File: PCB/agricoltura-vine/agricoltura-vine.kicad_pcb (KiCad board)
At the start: 2 copper layers, 110 x 70 mm, 106 parts, among them SW1 B3U-1000P, SW2 CVS-02TB, SW3 CVS-02TB, SW4 CVS-02TB, SW5 CVS-02TB, T1 BU2032SM-JJ-GTR, T10 B4B-PH-K-S(LF)(SN), T11 B4B-PH-K-S(LF)(SN), T12 B4B-PH-K-S(LF)(SN), T13 B4B-PH-K-S(LF)(SN), T14 B4B-PH-K-S(LF)(SN), T15 B4B-PH-K-S(LF)(SN), T16 1755736, T17 RJHSE-5381, T18 RJHSE-5381, T19 TSW-108-07-G-T, T2 20021121-00010C4LF, T20 TSW-108-07-G-T, T3 0675031020, T4 B4B-PH-K-S(LF)(SN), T5 B4B-PH-K-S(LF)(SN), T6 B4B-PH-K-S(LF)(SN), T7 B4B-PH-K-S(LF)(SN), T8 B4B-PH-K-S(LF)(SN), T9 B4B-PH-K-S(LF)(SN), U1 STM32F446RET6, U2 74HC4052D, U3 TCA9548APWR, U4 AP63203WU-7, U5 AP63205WU-7, U6 MAX3073EESD+, U7 MAX3073EESD+, U8 SN74LV541APWR, U9 TXB0108PWR, X1 ABM3B-8.000MHZ-B2-T, X2 ABS07-32.768KHZ-9-T

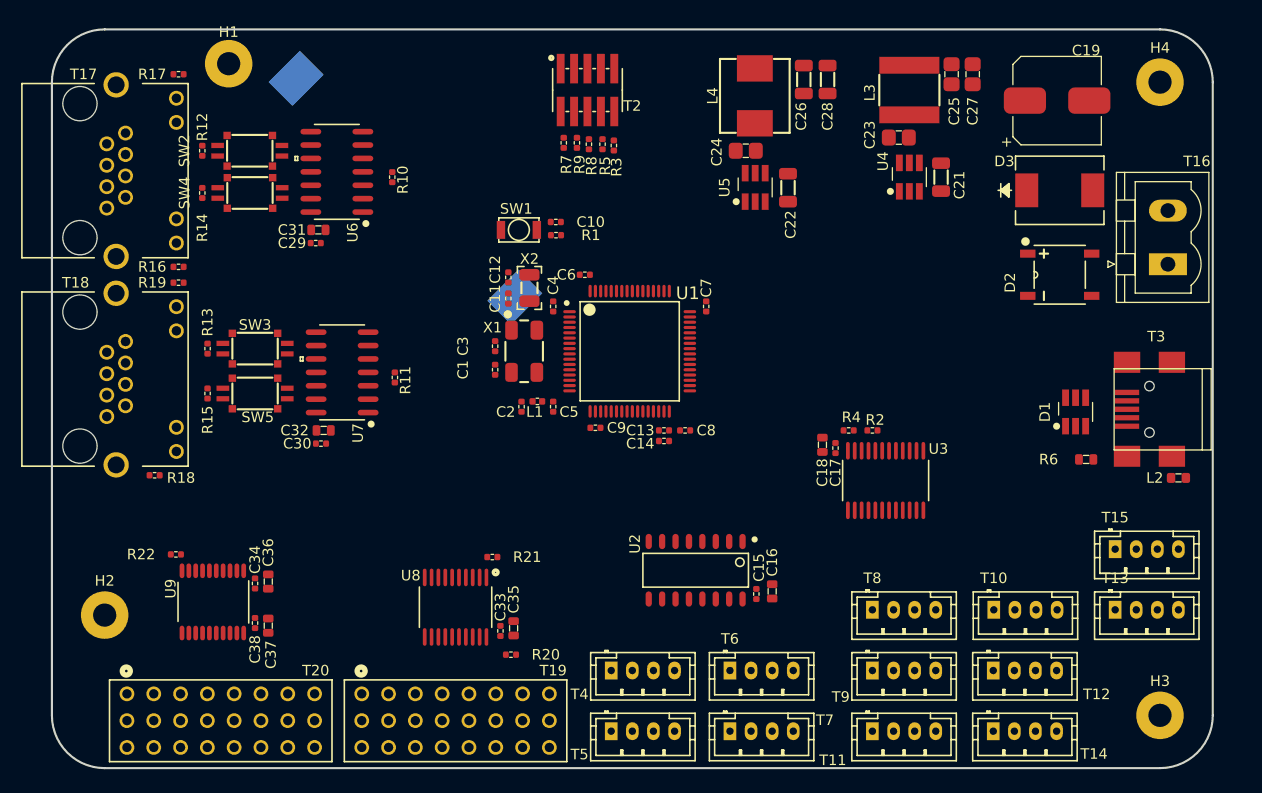
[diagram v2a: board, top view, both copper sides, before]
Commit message: Route Started Connectors Changed
Changed to QWIIC style connectors and adjusted pinning of RJ45s, but switching to screw terminal header in next commit. THis is a backup
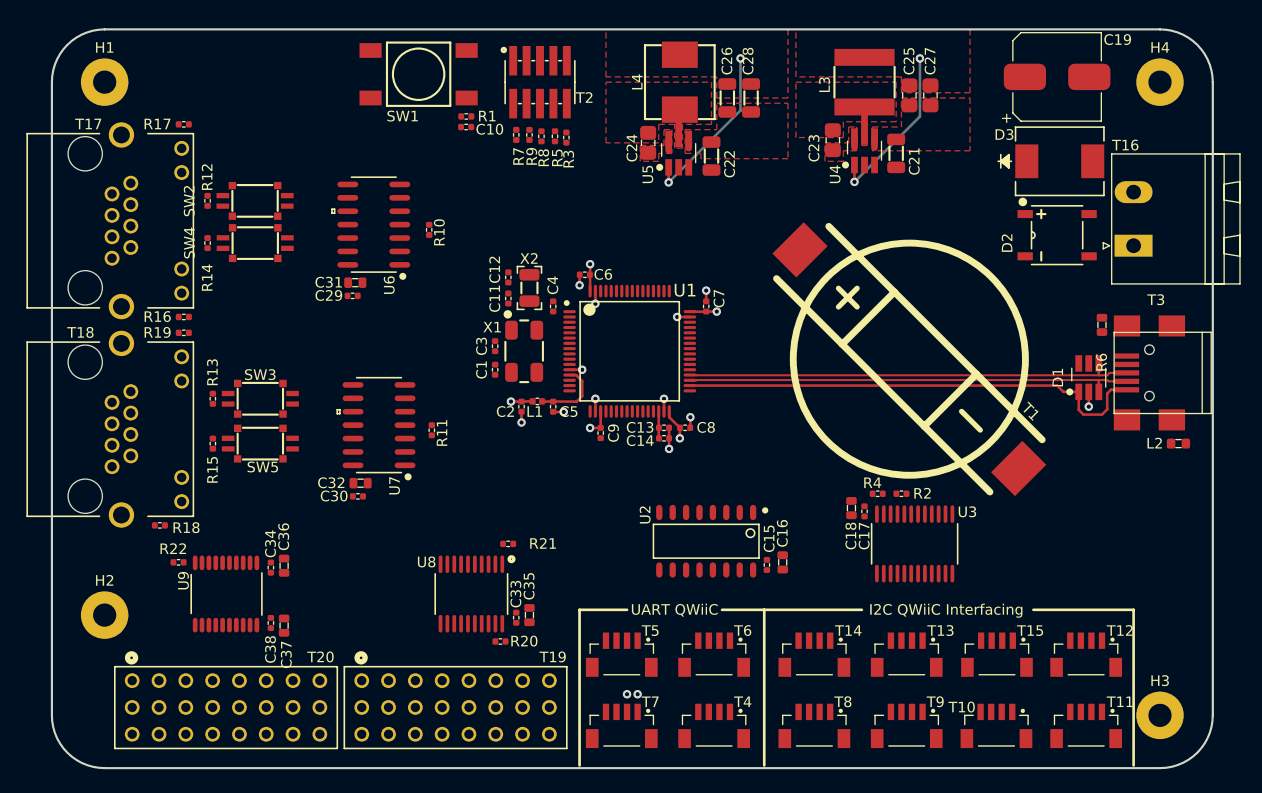
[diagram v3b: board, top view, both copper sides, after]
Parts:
- SW1: value B3U-1000P -> TL3301NF260QG; footprint AVR-KiCAD-Lib-Mech-Switches:B3U-1000P -> AVR-KiCAD-Lib-Mech-Switches:TL3301NF260QG
- T1: moved to F.Cu
- T10, T11, T12, T13, T14, T15, T4, T5, T6, T7, T8, T9: value B4B-PH-K-S(LF)(SN) -> BM04B-SRSS-TB(LF)(SN); footprint AVR-KiCAD-Lib-Connectors:B4B-PH-K-S(LF)(SN) -> AVR-KiCAD-Lib-Connectors:CONN_BM04B-SRSS-TB(LF)(SN)
- T16: value 1755736 -> 1757242; footprint growbox-KiCAD-Connectors:PhoenixContact_MSTBVA-G_02x5.08mm_Vertical -> AVR-KiCAD-Lib-Connectors:PhoenixContact_MSTBA-G_02x5.08mm_Angled
- moved T1 50.4 mm to (186.2, 96.2), turned to 315 degrees
- moved T11 20.3 mm to (203.0, 131.0), turned to 180 degrees
- moved T13 20.2 mm to (186.0, 124.2), turned to 180 degrees
- moved T14 18.4 mm to (177.2, 124.2), turned to 180 degrees
- moved SW1 17.5 mm to (139.8, 69.2)
- moved T15 15.0 mm to (194.6, 124.2), turned to 180 degrees
- moved R1 14.1 mm to (144.3, 73.2)
- moved R6 12.8 mm to (204.5, 93.0), turned to 90 degrees
- moved C10 12.4 mm to (144.2, 74.2), turned to 0 degrees
- moved T8 12.3 mm to (177.2, 131.0), turned to 180 degrees
- moved H1 11.9 mm to (110.0, 70.0)
- moved T4 11.1 mm to (167.8, 131.0), turned to 180 degrees
- moved T10 11.0 mm to (194.5, 131.0), turned to 180 degrees
- moved T7 10.3 mm to (159.0, 131.0), turned to 180 degrees
- moved C24 9.28 mm to (161.5, 75.8), turned to 90 degrees
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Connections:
- net Net-(C1-Pad1) renamed /STM32F446RET Controller/OSC_IN
- net Net-(C11-Pad2) renamed /STM32F446RET Controller/OSC32_OUT
- net Net-(C12-Pad2) renamed /STM32F446RET Controller/OSC32_IN
- net Net-(C13-Pad1) renamed /STM32F446RET Controller/VCAP1
- net Net-(C3-Pad1) renamed /STM32F446RET Controller/OSC_OUT
- net Net-(D1-Pad1) renamed /STM32F446RET Controller/VBUS
- net Net-(D1-Pad3) renamed /STM32F446RET Controller/D-
- net Net-(D1-Pad4) renamed /STM32F446RET Controller/D+
- net Net-(D1-Pad6) renamed /STM32F446RET Controller/ID
- net Net-(T4-Pad1) renamed /UART Sensor Interfaces/UARTS1_RX
- net Net-(T4-Pad2) renamed /UART Sensor Interfaces/UARTS1_TX
- net Net-(T5-Pad1) renamed /UART Sensor Interfaces/UARTS2_RX
- net Net-(T5-Pad2) renamed /UART Sensor Interfaces/UARTS2_TX
- net Net-(T6-Pad1) renamed /UART Sensor Interfaces/UARTS3_RX
- net Net-(T6-Pad2) renamed /UART Sensor Interfaces/UARTS3_TX
- net Net-(T7-Pad1) renamed /UART Sensor Interfaces/UARTS4_RX
- net Net-(T7-Pad2) renamed /UART Sensor Interfaces/UARTS4_TX
- C10 pad 1: Net-(C10-Pad1) -> /STM32F446RET Controller/NRST
- R1 pad 2: Net-(C10-Pad1) -> /STM32F446RET Controller/NRST
- SW1 pad 1: Net-(C10-Pad1) -> /STM32F446RET Controller/NRST
- SW1 pad 2: GND -> /STM32F446RET Controller/NRST
- SW2 pad 1: Net-(R12-Pad1) -> Net-(R12-Pad2)
- SW2 pad 2: Net-(R12-Pad2) -> Net-(R12-Pad1)
- SW3 pad 1: Net-(R13-Pad1) -> Net-(R13-Pad2)
- SW3 pad 2: Net-(R13-Pad2) -> Net-(R13-Pad1)
- SW4 pad 1: Net-(R14-Pad1) -> Net-(R14-Pad2)
- SW4 pad 2: Net-(R14-Pad2) -> Net-(R14-Pad1)
- SW5 pad 1: Net-(R15-Pad1) -> Net-(R15-Pad2)
- SW5 pad 2: Net-(R15-Pad2) -> Net-(R15-Pad1)
- T17 pad 2: Net-(SW2-Pad3) -> Net-(SW4-Pad3)
- T17 pad 3: Net-(SW2-Pad4) -> Net-(SW4-Pad4)
- T17 pad 6: Net-(SW4-Pad3) -> Net-(SW2-Pad3)
- T17 pad 7: Net-(SW4-Pad4) -> Net-(SW2-Pad4)
- T18 pad 2: Net-(SW3-Pad3) -> Net-(SW5-Pad3)
- T18 pad 3: Net-(SW3-Pad4) -> Net-(SW5-Pad4)
- T18 pad 6: Net-(SW5-Pad3) -> Net-(SW3-Pad3)
- T18 pad 7: Net-(SW5-Pad4) -> Net-(SW3-Pad4)
- U1 pad 7: Net-(C10-Pad1) -> /STM32F446RET Controller/NRST
- U6 pad 10: Net-(SW2-Pad4) -> Net-(SW2-Pad3)
- U6 pad 11: Net-(SW4-Pad3) -> Net-(SW4-Pad4)
- U6 pad 12: Net-(SW4-Pad4) -> Net-(SW4-Pad3)
- U6 pad 9: Net-(SW2-Pad3) -> Net-(SW2-Pad4)
- U7 pad 10: Net-(SW3-Pad4) -> Net-(SW3-Pad3)
- U7 pad 11: Net-(SW5-Pad3) -> Net-(SW5-Pad4)
- U7 pad 12: Net-(SW5-Pad4) -> Net-(SW5-Pad3)
- U7 pad 9: Net-(SW3-Pad3) -> Net-(SW3-Pad4)
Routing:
- net /STM32F446RET Controller/VBUS: track 0.00 -> 45.4 mm
- net /STM32F446RET Controller/D+: track 0.00 -> 42.6 mm
- net /STM32F446RET Controller/D-: track 0.00 -> 42.6 mm
- net +3V3: track 0.00 -> 28.6 mm, vias 0 -> 7
- net GND: track 0.00 -> 16.4 mm, vias 0 -> 12
- net +5V: track 0.00 -> 16.0 mm, vias 0 -> 2
- net /STM32F446RET Controller/VDDA: track 0.00 -> 6.88 mm
- net Net-(C24-Pad2): track 0.00 -> 2.82 mm
- net Net-(C23-Pad2): track 0.00 -> 2.80 mm
- net /STM32F446RET Controller/VCAP1: track 0.00 -> 2.56 mm
- net Net-(C23-Pad1): track 0.00 -> 1.12 mm
- net Net-(C24-Pad1): track 0.00 -> 1.07 mm
- net /UART Sensor Interfaces/UARTS4_TX: vias 0 -> 1
- net /UART Sensor Interfaces/UARTS4_RX: vias 0 -> 1
- added copper zone on F.Cu, net +3V3
- added copper zone on F.Cu, net +5V
- added copper zone on F.Cu, net GND
- added copper zone on In1.Cu, net GND
- added copper zone on F.Cu, net Net-(C23-Pad1)
- added copper zone on F.Cu, net Net-(C23-Pad2)
- added copper zone on F.Cu, net Net-(C24-Pad1)
- added copper zone on F.Cu, net Net-(C24-Pad2)
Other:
- copper layers 2 -> 4
- rule trace_min: 0.2 -> 0.1778
- board text added: "I2C QWiiC Interfacing"
- board text added: "UART QWiiC"

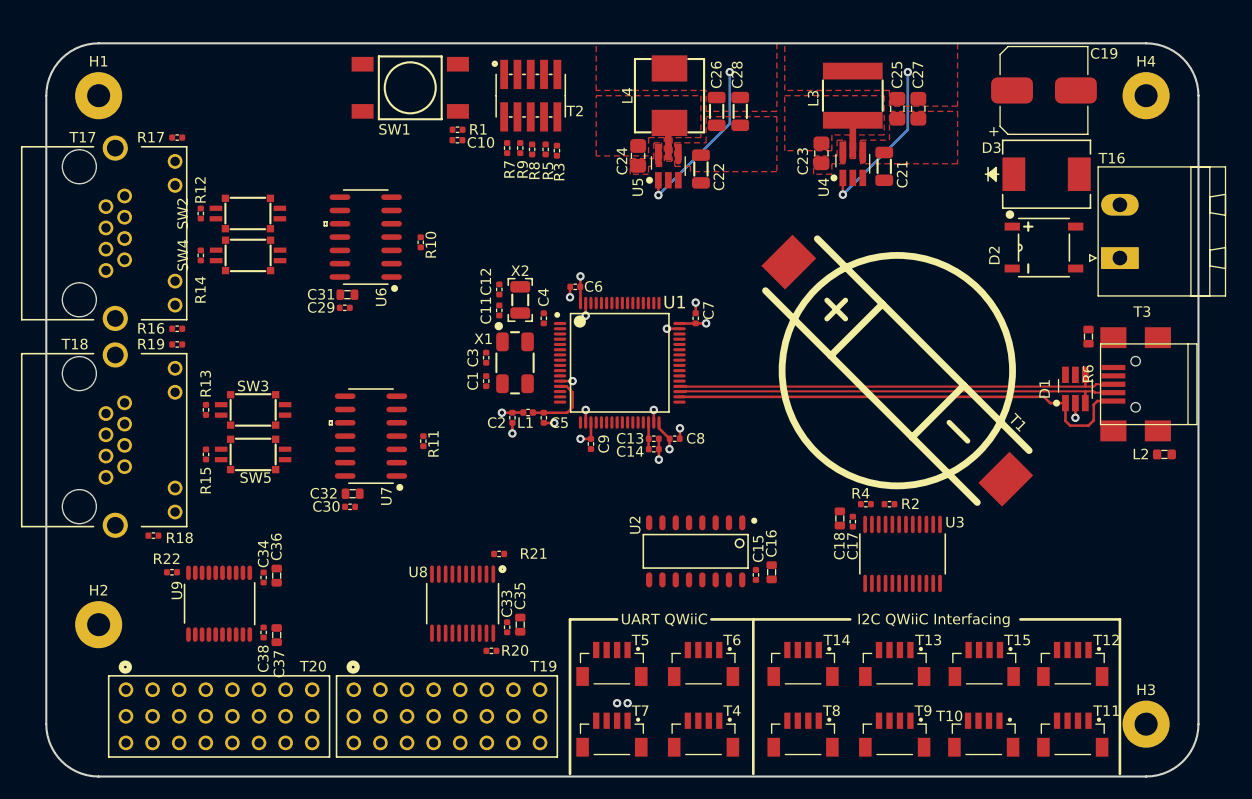
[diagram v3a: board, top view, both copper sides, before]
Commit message: Routing and New RS485
swapped over the RS485 chip to a new one and started routing the board.
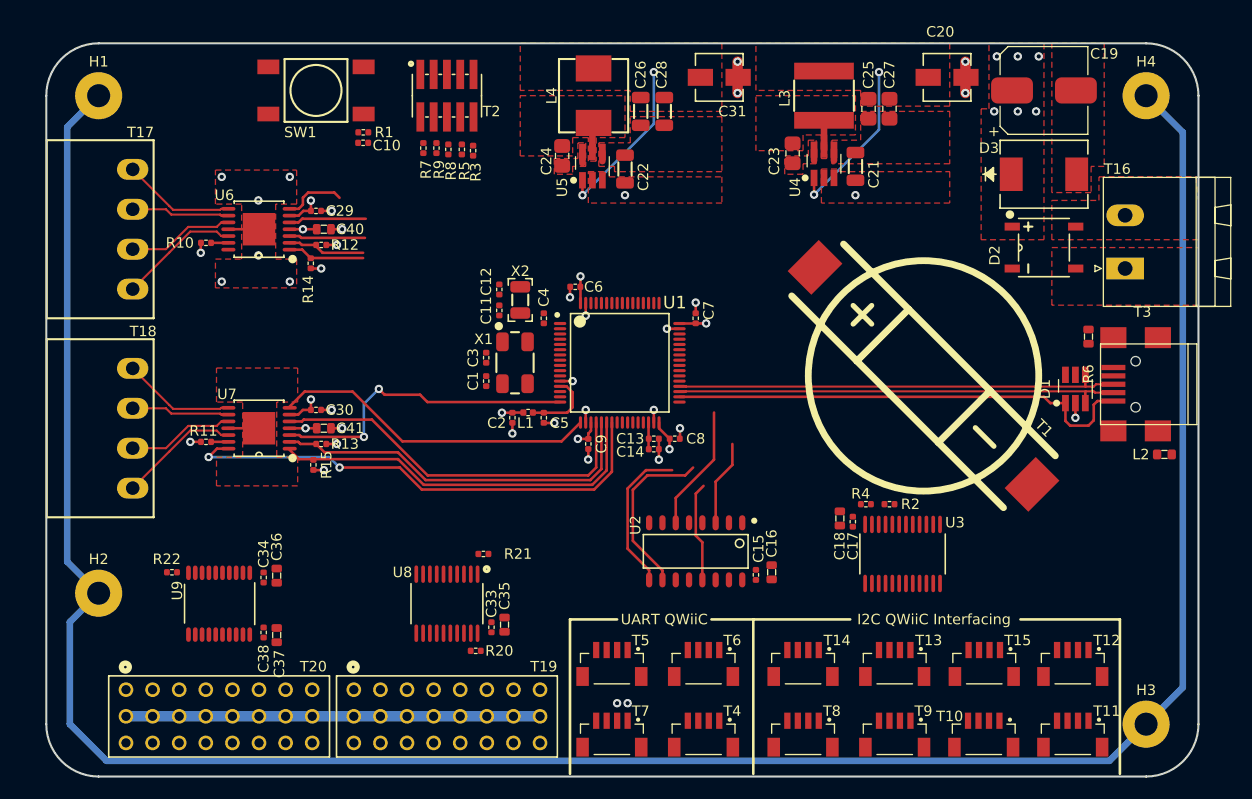
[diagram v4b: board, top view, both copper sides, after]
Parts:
- removed C32: GRM188R61A106KE69J, AVR-KiCAD-Lib-Capacitors:C0603
- removed R16, R17, R18, R19: RC0402FR-071KL, AVR-KiCAD-Lib-Resistors:R0402
- removed SW2, SW3, SW4, SW5: CVS-02TB, AVR-KiCAD-Lib-Mech-Switches:CVS-02TB
- added C20: UCM1C470MCL1GS, AVR-KiCAD-Lib-Capacitors:UCM1C470MCL1GS, F.Cu at (191.0, 68.2)
- added C40: CGA3E2X7R1H104K080AA, AVR-KiCAD-Lib-Capacitors:C0603, F.Cu at (131.5, 82.8)
- added C41: CGA3E2X7R1H104K080AA, AVR-KiCAD-Lib-Capacitors:C0603, F.Cu at (131.5, 101.8)
- C31: value GRM188R61A106KE69J -> UCM1C470MCL1GS; footprint AVR-KiCAD-Lib-Capacitors:C0603 -> AVR-KiCAD-Lib-Capacitors:UCM1C470MCL1GS
- R10, R11: value RC0402FR-074K7L -> RC0402FR-071KL
- R12, R13, R14, R15: value AC0402FR-07120RL -> RC0402FR-071KL
- T17, T18: value RJHSE-5381 -> 0395121004; footprint AVR-KiCAD-Lib-Connectors:AMPHENOL_RJHSE-5381 -> AVR-KiCAD-Lib-Connectors:0395121004
- U6, U7: value MAX3073EESD+ -> MAX13450EAUD+; footprint AVR-KiCAD-Lib-ICs:MAX3073EESD&plus_ -> AVR-KiCAD-Lib-ICs:MAX13450EAUD&plus_
- moved C31 41.1 mm to (169.2, 68.2)
- moved R11 20.8 mm to (120.2, 103.0), turned to 180 degrees
- moved R10 20.5 mm to (120.2, 84.0), turned to 180 degrees
- moved R12 11.9 mm to (131.2, 84.2), turned to 180 degrees
- moved R13 11.5 mm to (131.2, 103.2), turned to 180 degrees
- moved U7 10.7 mm to (125.3, 101.8)
- moved R14 10.5 mm to (130.2, 86.0)
- moved R15 10.3 mm to (130.5, 105.2)
- moved U6 10.2 mm to (125.3, 82.8)
- moved C30 9.80 mm to (130.8, 100.0)
- moved C29 9.65 mm to (130.8, 81.0)
- moved C10 9.00 mm to (135.2, 74.5)
- moved R1 9.00 mm to (135.3, 73.5)
- moved SW1 9.00 mm to (130.8, 69.5)
- moved R3 8.00 mm to (145.8, 75.2)
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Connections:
- net Net-(D2-Pad2) renamed /Power Supply/24VAC-
- net Net-(D2-Pad4) renamed /Power Supply/24VAC+
- C31 pad 1: +3V3 -> +5V
- H1 pad 1: Net-(H1-Pad1) -> Earth
- H2 pad 1: Net-(H2-Pad1) -> Earth
- H3 pad 1: Net-(H3-Pad1) -> Earth
- H4 pad 1: Net-(H4-Pad1) -> Earth
- R10 pad 1: +3V3 -> Net-(R10-Pad1)
- R10 pad 2: /RS485 Interface/RS485_UART_EN1 -> GND
- R11 pad 1: +3V3 -> Net-(R11-Pad1)
- R11 pad 2: /RS485 Interface/RS485_UART_EN2 -> GND
- R12 pad 1: Net-(R12-Pad1) -> +3V3
- R12 pad 2: Net-(R12-Pad2) -> /RS485 Interface/RS485_RE1
- R13 pad 1: Net-(R13-Pad1) -> +3V3
- R13 pad 2: Net-(R13-Pad2) -> /RS485 Interface/RS485_RE2
- R14 pad 1: Net-(R14-Pad1) -> +3V3
- R14 pad 2: Net-(R14-Pad2) -> /RS485 Interface/RS485_DE1
- R15 pad 1: Net-(R15-Pad1) -> +3V3
- R15 pad 2: Net-(R15-Pad2) -> /RS485 Interface/RS485_DE2
- R2 pad 2: /I2C Sensor Interfaces/I2C_SENSE1_SCL -> /STM32F446RET Controller/I2C_SENSE1_SCL
- R4 pad 2: /I2C Sensor Interfaces/I2C_SENSE1_SDA -> /STM32F446RET Controller/I2C_SENSE1_SDA
- T17 pad 1: Net-(T17-Pad1) -> /RS485 Interface/RS485_RX1-
- T17 pad 2: Net-(SW4-Pad3) -> /RS485 Interface/RS485_RX1+
- T17 pad 3: Net-(SW4-Pad4) -> /RS485 Interface/RS485_TX1-
- T17 pad 4: Net-(T17-Pad4) -> /RS485 Interface/RS485_TX1+
- T18 pad 1: Net-(T18-Pad1) -> /RS485 Interface/RS485_RX2-
- T18 pad 2: Net-(SW5-Pad3) -> /RS485 Interface/RS485_RX2+
- T18 pad 3: Net-(SW5-Pad4) -> /RS485 Interface/RS485_TX2-
- T18 pad 4: Net-(T18-Pad4) -> /RS485 Interface/RS485_TX2+
- T19 pad 11: +3V3 -> +5V
- T19 pad 14: +3V3 -> +5V
- T19 pad 17: +3V3 -> +5V
- T19 pad 2: +3V3 -> +5V
- T19 pad 20: +3V3 -> +5V
- T19 pad 23: +3V3 -> +5V
- T19 pad 5: +3V3 -> +5V
- T19 pad 8: +3V3 -> +5V
- T20 pad 11: +3V3 -> +5V
- T20 pad 14: +3V3 -> +5V
- T20 pad 17: +3V3 -> +5V
- T20 pad 2: +3V3 -> +5V
- T20 pad 20: +3V3 -> +5V
- T20 pad 23: +3V3 -> +5V
- T20 pad 5: +3V3 -> +5V
- T20 pad 8: +3V3 -> +5V
- U1 pad 20: /RS485 Interface/RS485_UART_EN1 -> /RS485 Interface/RS485_TERM_EN2
- U1 pad 21: /RS485 Interface/RS485_UART_EN2 -> /RS485 Interface/RS485_RE2
- U1 pad 22: Net-(U1-Pad22) -> /RS485 Interface/RS485_DE2
- U1 pad 23: Net-(U1-Pad23) -> /RS485 Interface/RS485_SL_RATE2
- U1 pad 57: /I2C Sensor Interfaces/I2C_MUX1_RESET -> /STM32F446RET Controller/I2C_MUX1_RESET
- U1 pad 58: /I2C Sensor Interfaces/I2C_SENSE1_SCL -> /STM32F446RET Controller/I2C_SENSE1_SCL
- U1 pad 59: /I2C Sensor Interfaces/I2C_SENSE1_SDA -> /STM32F446RET Controller/I2C_SENSE1_SDA
- U6 pad 1: Net-(U6-Pad1) -> /RS485 Interface/RS485_DE1
- U6 pad 10: Net-(SW2-Pad3) -> /RS485 Interface/RS485_TX1-
- U6 pad 11: Net-(SW4-Pad4) -> GND
- U6 pad 12: Net-(SW4-Pad3) -> /RS485 Interface/RS485_TX1+
- U6 pad 13: Net-(U6-Pad13) -> Net-(R10-Pad1)
- U6 pad 14: +3V3 -> /RS485 Interface/RS485_SL_RATE1
- U6 pad 2: /RS485 Interface/RS485_UART_RX1 -> /RS485 Interface/RS485_RE1
- U6 pad 3: GND -> /RS485 Interface/RS485_UART_TX1
- U6 pad 4: /RS485 Interface/RS485_UART_EN1 -> +5V
- U6 pad 5: /RS485 Interface/RS485_UART_TX1 -> /RS485 Interface/RS485_TERM_EN1
- U6 pad 6: GND -> +3V3
- U6 pad 7: GND -> /RS485 Interface/RS485_UART_RX1
- U6 pad 8: Net-(U6-Pad8) -> /RS485 Interface/RS485_RX1-
- U6 pad 9: Net-(SW2-Pad4) -> /RS485 Interface/RS485_RX1+
- U7 pad 1: Net-(U7-Pad1) -> /RS485 Interface/RS485_DE2
- U7 pad 10: Net-(SW3-Pad3) -> /RS485 Interface/RS485_TX2-
- U7 pad 11: Net-(SW5-Pad4) -> GND
- U7 pad 12: Net-(SW5-Pad3) -> /RS485 Interface/RS485_TX2+
- U7 pad 13: Net-(U7-Pad13) -> Net-(R11-Pad1)
- U7 pad 14: +3V3 -> /RS485 Interface/RS485_SL_RATE2
- U7 pad 2: /RS485 Interface/RS485_UART_RX2 -> /RS485 Interface/RS485_RE2
- U7 pad 3: GND -> /RS485 Interface/RS485_UART_TX2
- U7 pad 4: /RS485 Interface/RS485_UART_EN2 -> +5V
- U7 pad 5: /RS485 Interface/RS485_UART_TX2 -> /RS485 Interface/RS485_TERM_EN2
- U7 pad 6: GND -> +3V3
- U7 pad 7: GND -> /RS485 Interface/RS485_UART_RX2
- U7 pad 8: Net-(U7-Pad8) -> /RS485 Interface/RS485_RX2-
- U7 pad 9: Net-(SW3-Pad4) -> /RS485 Interface/RS485_RX2+
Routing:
- net Earth: track 0.00 -> 232.2 mm
- net /RS485 Interface/RS485_SL_RATE2: track 0.00 -> 47.4 mm, vias 0 -> 2
- net +5V: track 16.0 -> 60.6 mm, vias 2 -> 4
- net /RS485 Interface/RS485_DE2: track 0.00 -> 37.0 mm
- net /RS485 Interface/RS485_RE2: track 0.00 -> 36.3 mm
- net /RS485 Interface/RS485_TERM_EN2: track 0.00 -> 36.3 mm
- net /RS485 Interface/RS485_UART_RX2: track 0.00 -> 31.2 mm
- net /RS485 Interface/RS485_UART_TX2: track 0.00 -> 30.3 mm, vias 0 -> 2
- net GND: track 16.4 -> 35.4 mm, vias 12 -> 29
- net /STM32F446RET Controller/USW1_S0: track 0.00 -> 16.4 mm
- net /STM32F446RET Controller/USW1_S1: track 0.00 -> 14.6 mm
- net /STM32F446RET Controller/USW1_EN: track 0.00 -> 12.0 mm
- net /RS485 Interface/RS485_TX2+: track 0.00 -> 11.6 mm
- net /RS485 Interface/RS485_TX1+: track 0.00 -> 11.6 mm
- net /RS485 Interface/RS485_RX2-: track 0.00 -> 10.8 mm
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- added copper zone on F.Cu, net +24V
- added copper zone on In2.Cu, net +24V
- added copper zone on In2.Cu, net +3V3
- added copper zone on F.Cu, net /Power Supply/24VAC+
- added copper zone on F.Cu, net /Power Supply/24VAC-
